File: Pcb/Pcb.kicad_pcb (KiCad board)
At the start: 2 copper layers, 152.3 x 104.7 mm, 150 parts, among them J1 TRRS, Q1 2N7002, SW1 SW_Push, SW10 SW_Push, SW11 SW_Push, SW12 SW_Push, SW13 SW_Push, SW14 SW_Push, SW15 SW_Push, SW16 SW_Push, SW17 SW_Push, SW18 SW_Push, SW19 SW_Push, SW2 SW2, SW20 SW_Push, SW21 SW_Push, SW22 SW_Push, SW23 SW_Push, SW24 SW_Push, SW25 SW_Push, SW26 SW_Push, SW27 SW_Push, SW28 SW_Push, SW29 SW_Push, SW3 SW_Push, SW4 SW_Push, SW5 SW_Push, SW6 SW_Push, SW7 SW_Push, SW8 SW_Push, SW9 SW_Push, U1 ProMicro

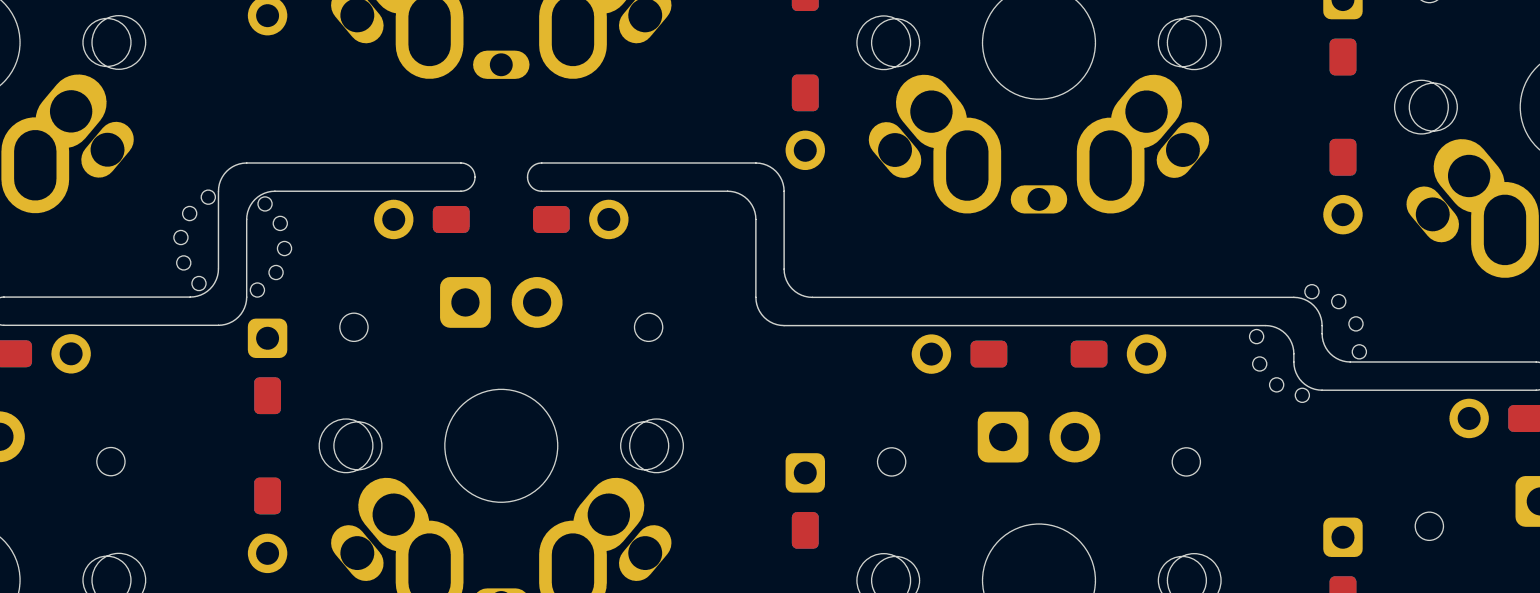
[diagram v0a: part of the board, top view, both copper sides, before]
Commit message: Add more break holes
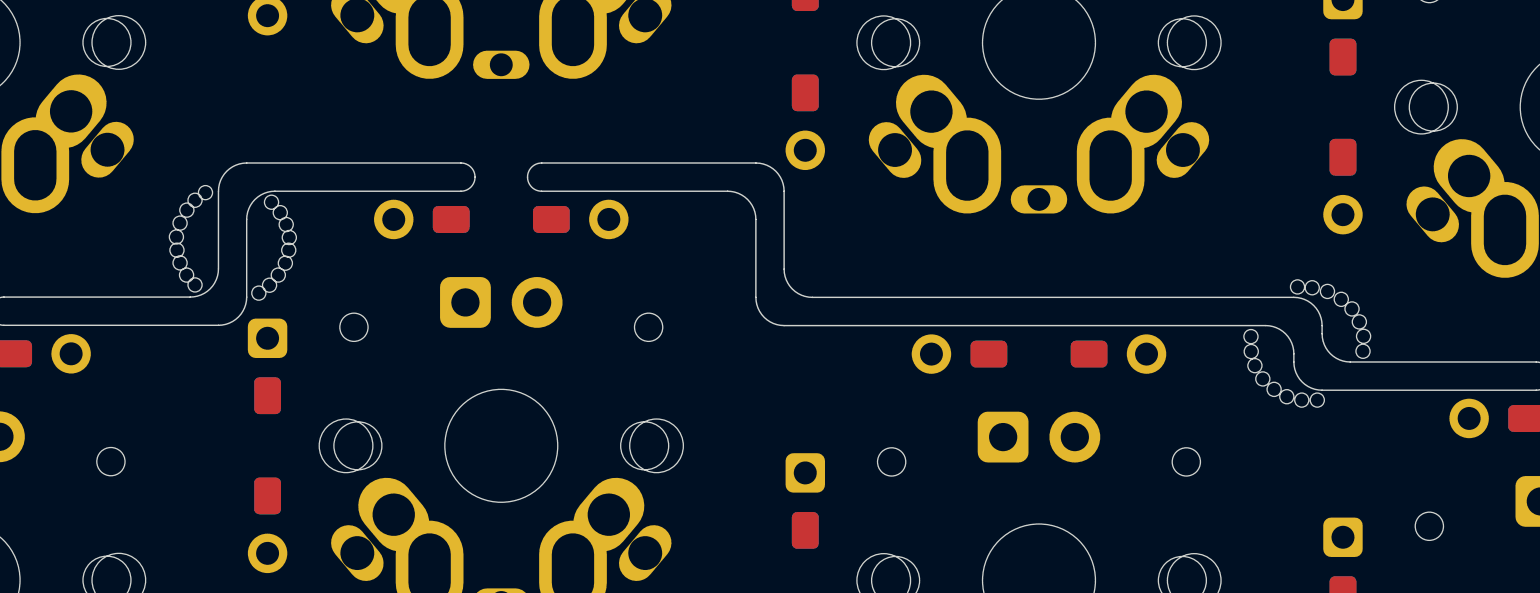
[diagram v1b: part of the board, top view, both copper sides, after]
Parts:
- added HB1: HoleBreak, Used_Footprints:HoleBreak, F.Cu at (191.1, 53.0)
- added HB11: HoleBreak, Used_Footprints:HoleBreak, F.Cu at (190.7, 56.9)
- added HB13: HoleBreak, Used_Footprints:HoleBreak, F.Cu at (189.8, 56.3)
- added HB15: HoleBreak, Used_Footprints:HoleBreak, F.Cu at (189.4, 55.3)
- added HB18: HoleBreak, Used_Footprints:HoleBreak, F.Cu at (155.0, 50.4)
- added HB20: HoleBreak, Used_Footprints:HoleBreak, F.Cu at (155.3, 51.3)
- added HB22: HoleBreak, Used_Footprints:HoleBreak, F.Cu at (155.2, 52.2)
- added HB24: HoleBreak, Used_Footprints:HoleBreak, F.Cu at (154.7, 53.0)
- added HB27: HoleBreak, Used_Footprints:HoleBreak, F.Cu at (151.7, 52.6)
- added HB29: HoleBreak, Used_Footprints:HoleBreak, F.Cu at (151.4, 51.7)
- added HB3: HoleBreak, Used_Footprints:HoleBreak, F.Cu at (192.1, 53.2)
- added HB31: HoleBreak, Used_Footprints:HoleBreak, F.Cu at (151.5, 50.8)
- added HB33: HoleBreak, Used_Footprints:HoleBreak, F.Cu at (152.0, 50.0)
- added HB5: HoleBreak, Used_Footprints:HoleBreak, F.Cu at (193.0, 53.8)
- added HB7: HoleBreak, Used_Footprints:HoleBreak, F.Cu at (193.4, 54.8)
- added HB9: HoleBreak, Used_Footprints:HoleBreak, F.Cu at (191.8, 57.0)
- moved HB17 0.24 mm to (155.2, 50.2)
- moved HB19 0.21 mm to (155.2, 50.8)
- moved HB16 0.20 mm to (189.4, 54.8)
- moved HB34 0.19 mm to (152.4, 49.7)
- moved HB12 0.18 mm to (190.2, 56.7)
- moved HB14 0.18 mm to (189.6, 55.8)
- moved HB10 0.17 mm to (191.2, 57.0)
- moved HB21 0.16 mm to (155.3, 51.7)
- moved HB30 0.16 mm to (151.3, 51.3)
- moved HB32 0.16 mm to (151.7, 50.3)
- moved HB26 0.15 mm to (152.0, 53.0)
- moved HB2 0.14 mm to (191.6, 53.1)
- moved HB6 0.14 mm to (193.3, 54.3)
- moved HB8 0.13 mm to (193.4, 55.3)
- moved HB28 0.13 mm to (151.5, 52.2)
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- renumbered HB18 to HB10, HB17 to HB12, HB16 to HB14, HB15 to HB16, HB6 to HB17, HB7 to HB19, HB11 to HB2, HB8 to HB21, HB9 to HB23, HB10 to HB25, HB5 to HB26, HB4 to HB28, HB3 to HB30, HB2 to HB32, HB1 to HB34, HB12 to HB4, HB13 to HB6, HB14 to HB8

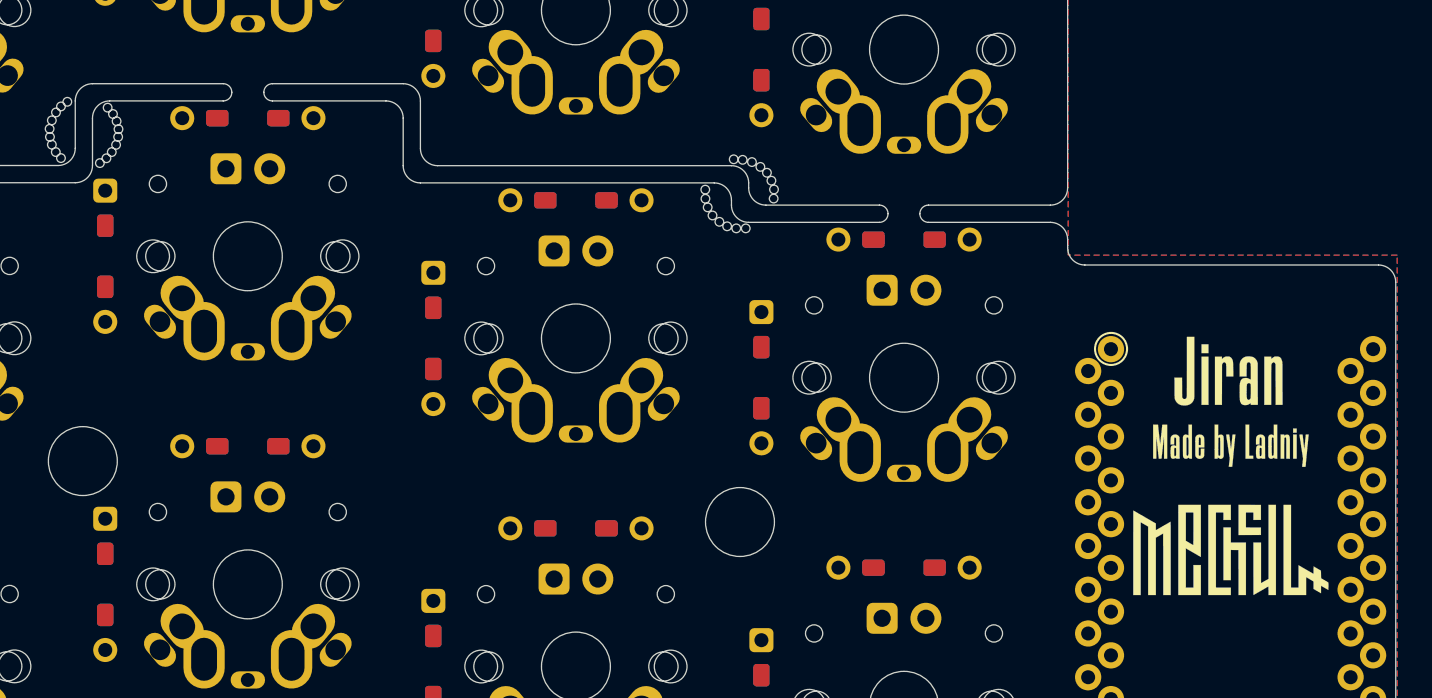
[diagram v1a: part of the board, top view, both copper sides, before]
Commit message: Remove old logo silkscreen
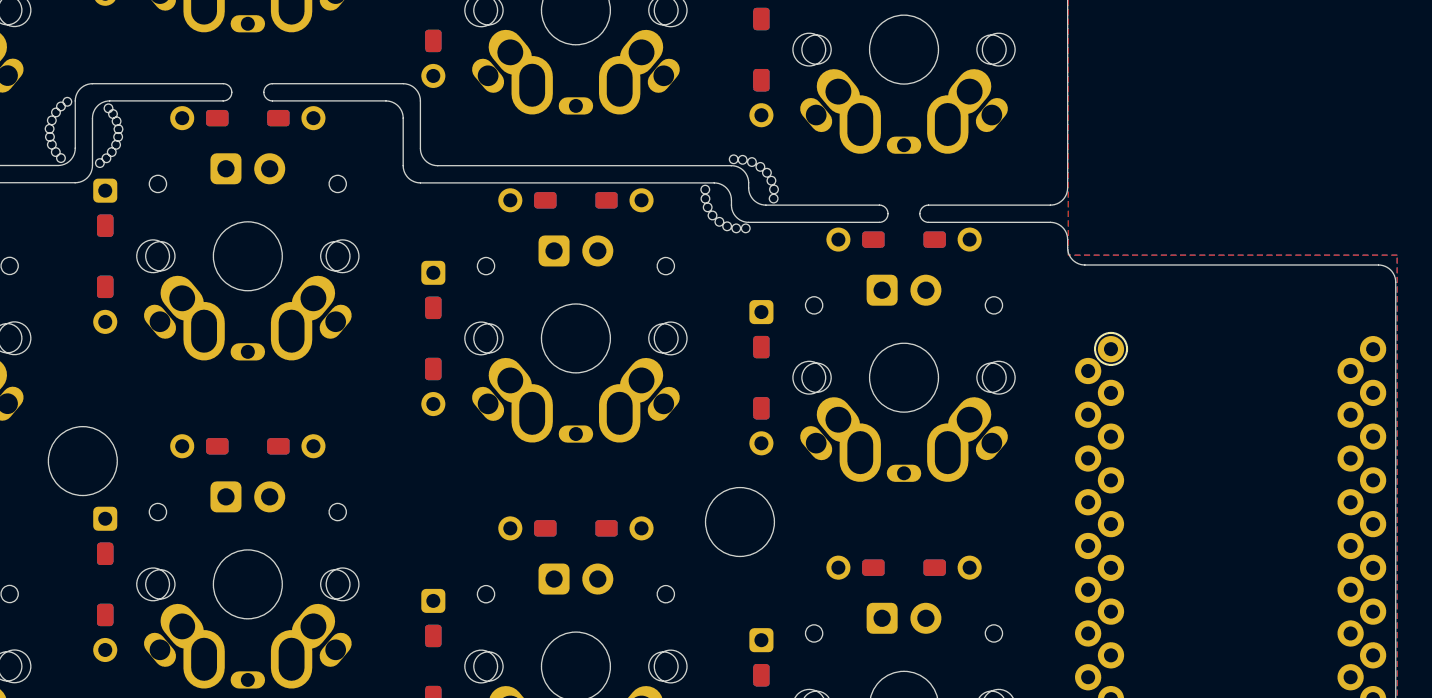
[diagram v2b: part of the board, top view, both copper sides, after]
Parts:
- removed G1, G2: LOGO, 1symblos:Silkscreen
- moved HB17 0.06 mm to (155.3, 50.2)

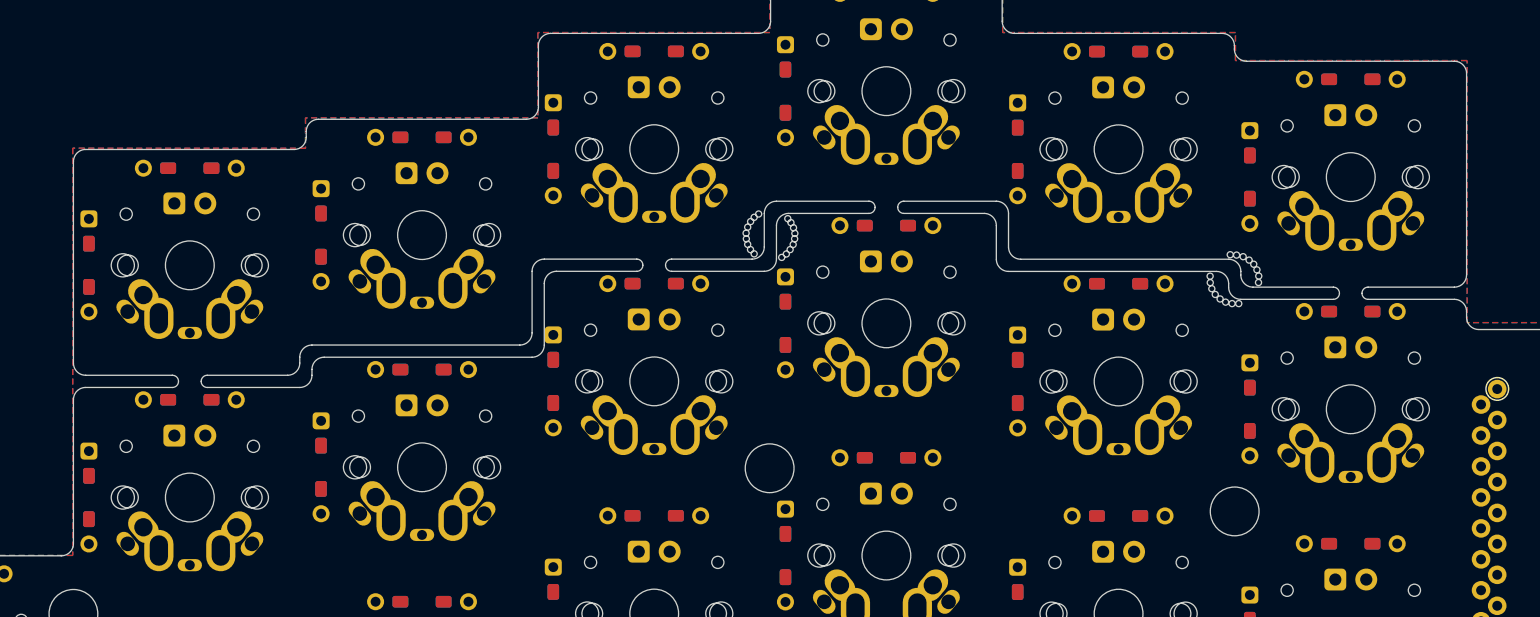
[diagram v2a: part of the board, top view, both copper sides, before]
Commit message: Delete breakoff cuts
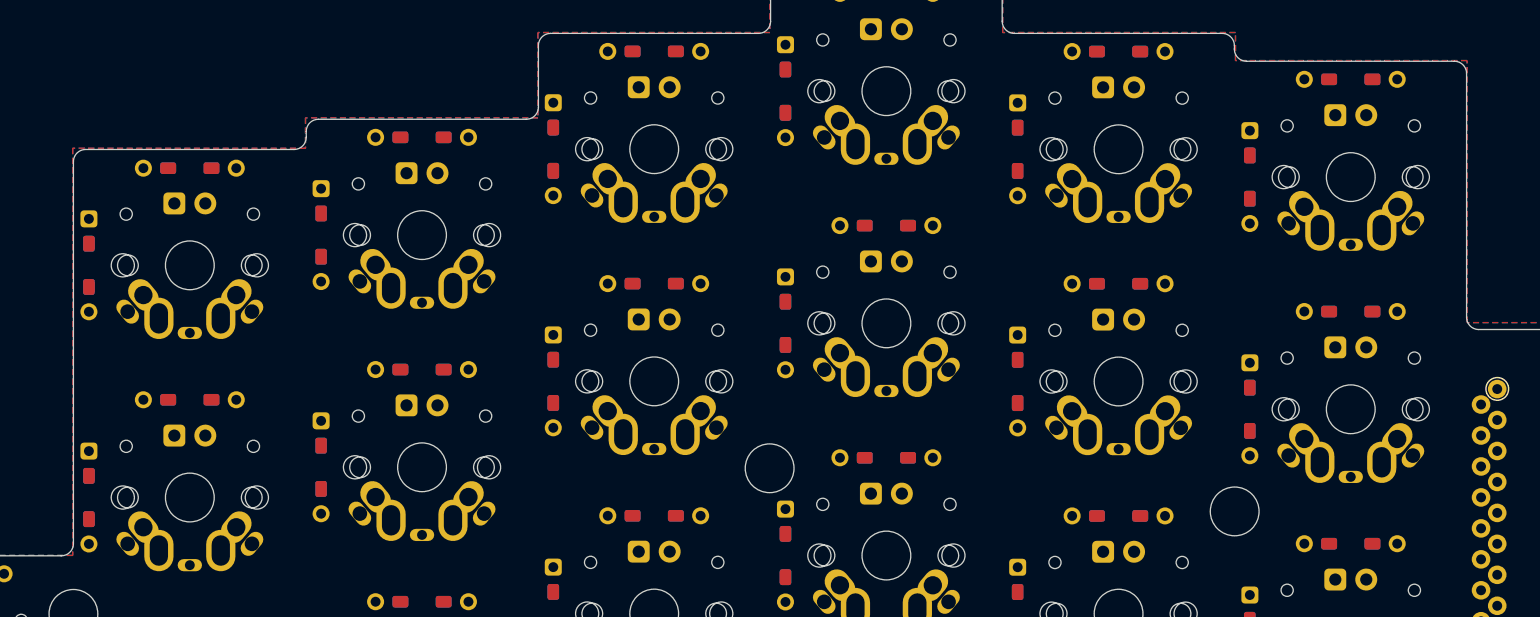
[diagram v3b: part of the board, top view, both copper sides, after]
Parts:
- removed HB1, HB10, HB11, HB12, HB13, HB14, HB15, HB16, HB17, HB18, HB19, HB2, HB20, HB21, HB22, HB23, HB24, HB25, HB26, HB27, HB28, HB29, HB3, HB30, HB31, HB32, HB33, HB34, HB4, HB5, HB6, HB7, HB8, HB9: HoleBreak, Used_Footprints:HoleBreak
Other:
- outline, holes or cut-outs redrawn

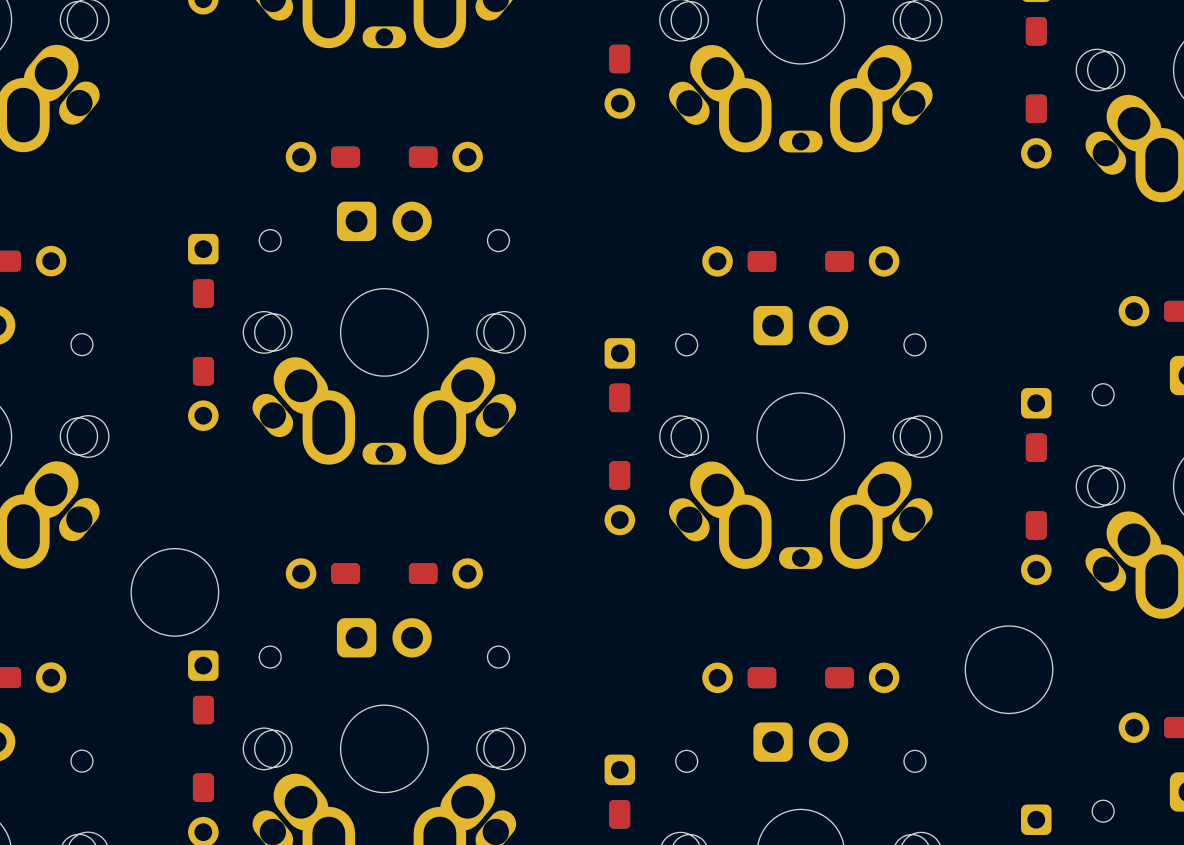
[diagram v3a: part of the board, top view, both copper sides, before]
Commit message: Remove hole for Jian mode
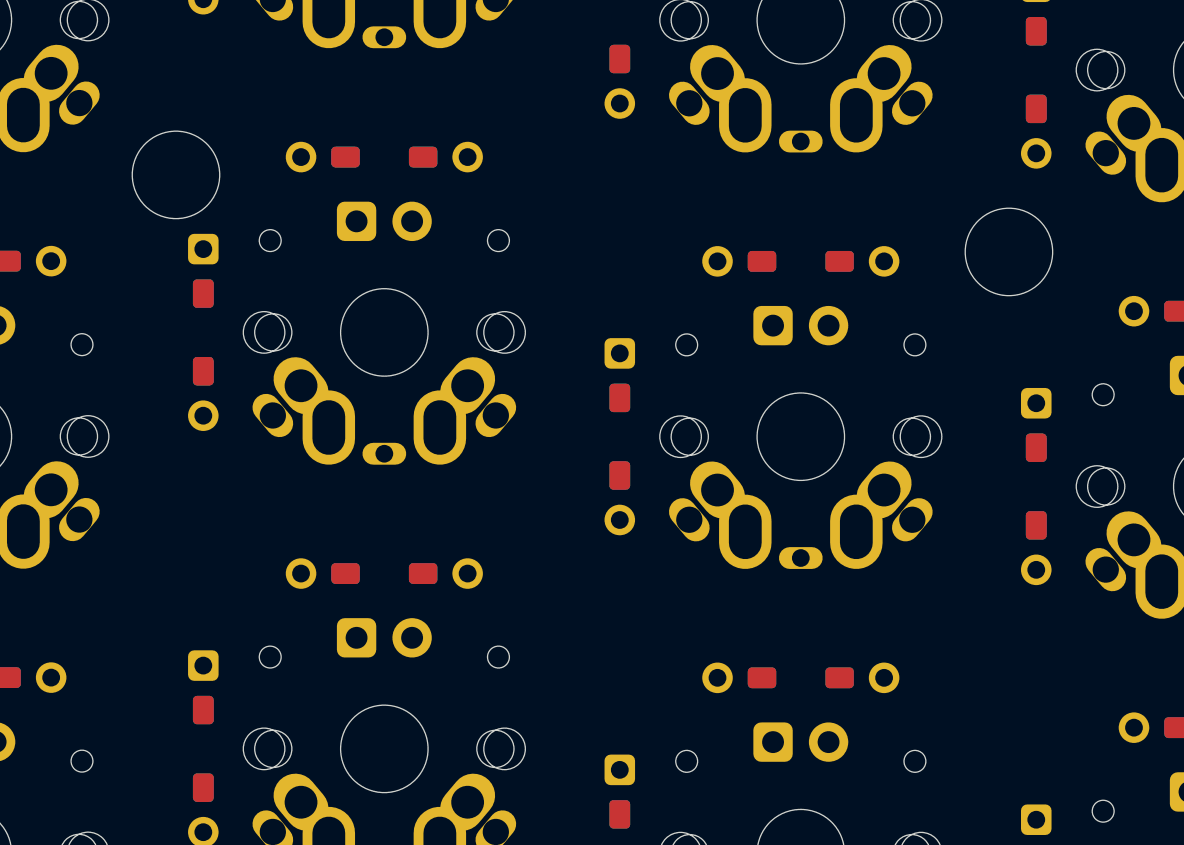
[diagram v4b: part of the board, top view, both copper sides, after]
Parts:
- moved H6 19.1 mm to (191.4, 55.0)
- moved H3 19.1 mm to (153.3, 51.5)
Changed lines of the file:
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@@
   )
   (module Used_Footprints:MountHole (layer F.Cu)
-    (at 153.28 70.5512)
+    (at 153.33 51.45525)
     (fp_text reference H3 (at 0.5 -2.77) (layer F.SilkS) hide
       (effects (font (size 1 1) (thickness 0.15)))
@@
   )
   (module Used_Footprints:MountHole (layer F.Cu)
-    (at 191.435 74.0895)
+    (at 191.43 54.9795)
     (fp_text reference H6 (at 0.5 -2.77) (layer F.SilkS) hide
       (effects (font (size 1 1) (thickness 0.15)))

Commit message: Move hole for mount
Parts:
- renumbered H6 to H4, H7 to H5

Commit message: Route tracks
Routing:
- net VCC: track 0.00 -> 628.5 mm, vias 0 -> 6
- net /LEDOut: track 0.00 -> 573.1 mm, vias 0 -> 1
- net /rowA: track 0.00 -> 331.1 mm, vias 0 -> 7
- net /col0: track 0.00 -> 259.0 mm, vias 0 -> 4
- net /rowB: track 0.00 -> 249.8 mm, vias 0 -> 5
- net /rowE: track 0.00 -> 237.2 mm
- net /col1: track 0.00 -> 202.2 mm, vias 0 -> 3
- net /col4: track 0.00 -> 195.9 mm, vias 0 -> 7
- net /col5: track 0.00 -> 191.7 mm, vias 0 -> 8
- net /col3: track 0.00 -> 188.4 mm, vias 0 -> 1
- net /col2: track 0.00 -> 185.0 mm, vias 0 -> 1
- net /rowD: track 0.00 -> 182.8 mm, vias 0 -> 1
- net GND: track 0.00 -> 164.3 mm, vias 0 -> 5
- net /rowC: track 0.00 -> 163.4 mm
- net /SCROLL: track 0.00 -> 100.5 mm, vias 0 -> 3
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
